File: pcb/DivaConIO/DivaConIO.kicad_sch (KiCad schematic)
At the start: 33 parts, among them J1 DPad Buttons, J10 SWD, J2 Slider i2c, J3 Display i2c, J4 Face Buttons, J5 Button LEDs, J6 L Buttons, J7 Fn Buttons, J8 R Buttons, J9 Slider LEDs, Q1 BC847, Q2 BC847, Q3 BC847, Q4 BC847, SW1 Reset, U1 Pico, U2 SN74LVC1T45DCK

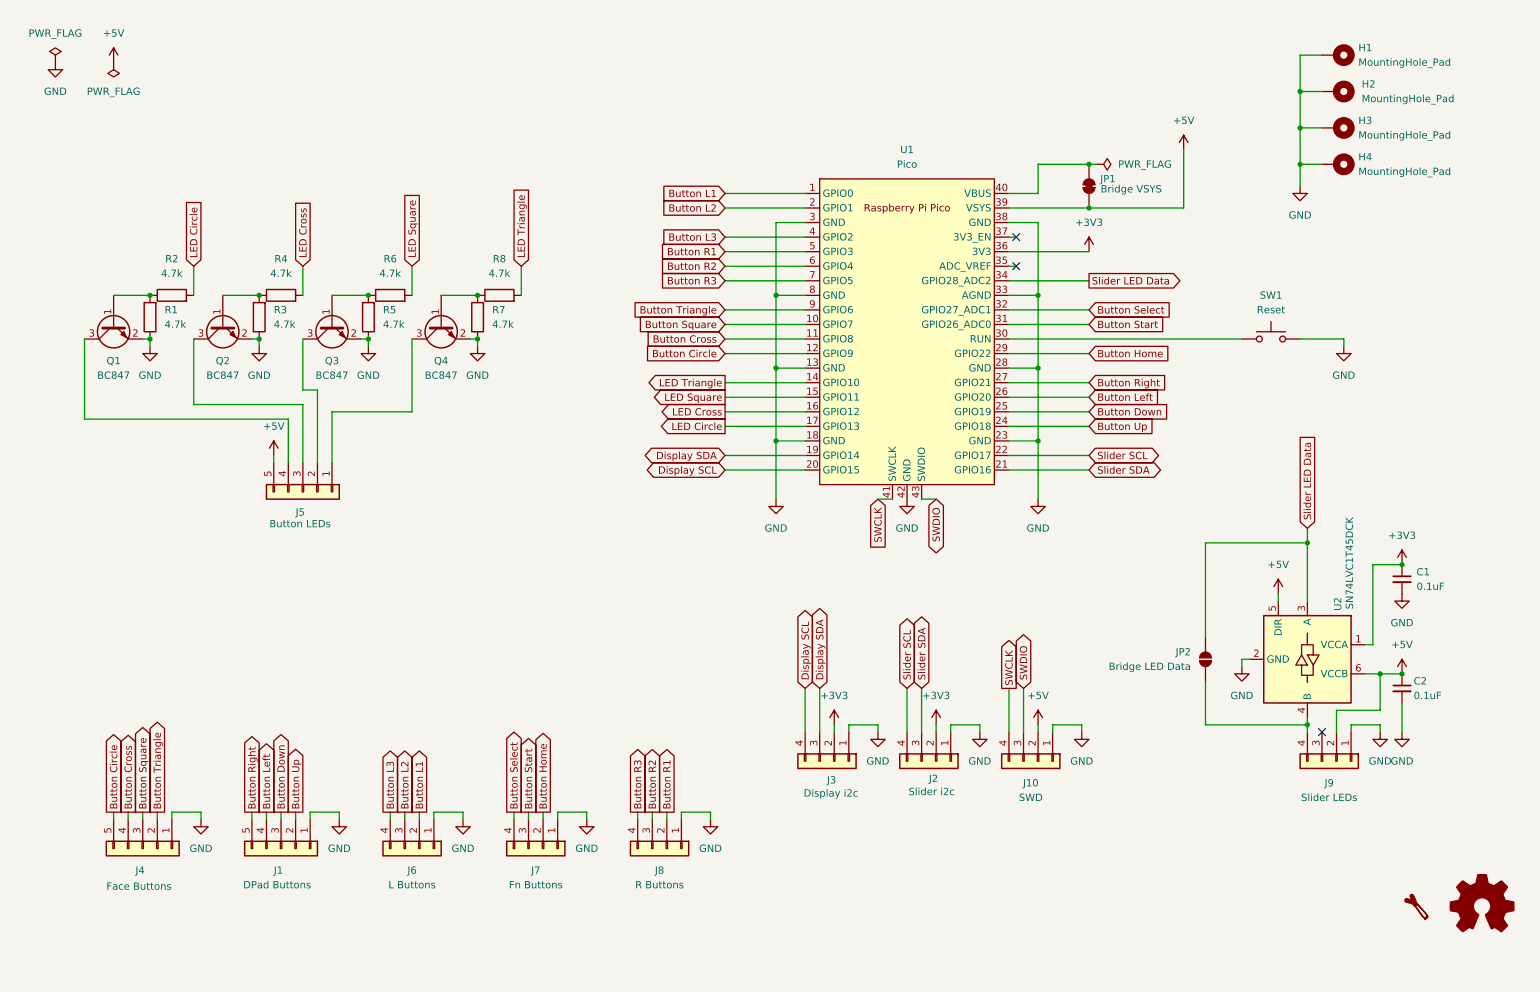
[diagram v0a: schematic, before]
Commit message: relaid out IO board
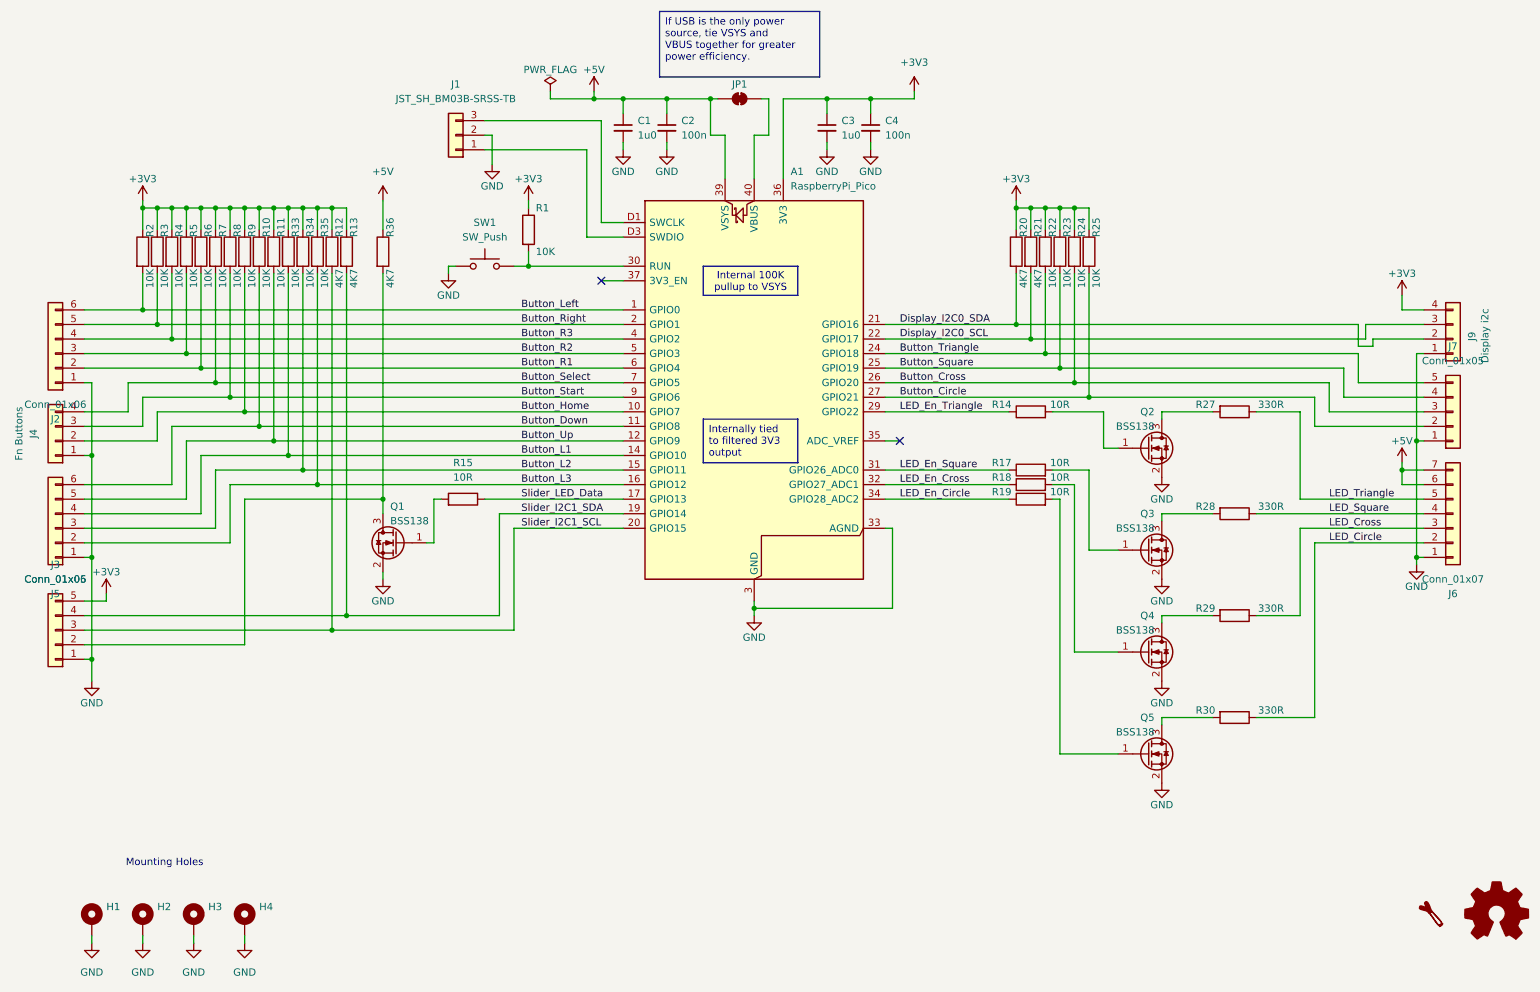
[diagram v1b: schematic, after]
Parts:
- removed J1: DPad Buttons, Connector_JST:JST_PH_B5B-PH-K_1x05_P2.00mm_Vertical, symbol Connector_Generic:Conn_01x05
- removed J10: SWD, Connector_JST:JST_PH_B4B-PH-K_1x04_P2.00mm_Vertical, symbol Connector_Generic:Conn_01x04
- removed J2: Slider i2c, Connector_JST:JST_PH_B4B-PH-K_1x04_P2.00mm_Vertical, symbol Connector_Generic:Conn_01x04
- removed J4: Face Buttons, Connector_JST:JST_PH_B5B-PH-K_1x05_P2.00mm_Vertical, symbol Connector_Generic:Conn_01x05
- removed J5: Button LEDs, Connector_JST:JST_PH_B5B-PH-K_1x05_P2.00mm_Vertical, symbol Connector_Generic:Conn_01x05
- removed J6: L Buttons, Connector_JST:JST_PH_B4B-PH-K_1x04_P2.00mm_Vertical, symbol Connector_Generic:Conn_01x04
- removed J7: Fn Buttons, Connector_JST:JST_PH_B4B-PH-K_1x04_P2.00mm_Vertical, symbol Connector_Generic:Conn_01x04
- removed J8: R Buttons, Connector_JST:JST_PH_B4B-PH-K_1x04_P2.00mm_Vertical, symbol Connector_Generic:Conn_01x04
- removed J9: Slider LEDs, Connector_JST:JST_PH_B4B-PH-K_1x04_P2.00mm_Vertical, symbol Connector_Generic:Conn_01x04
- removed JP2: Bridge LED Data, Jumper:SolderJumper-2_P1.3mm_Open_RoundedPad1.0x1.5mm, symbol Jumper:SolderJumper_2_Open
- removed Q1, Q2, Q3, Q4: BC847, Package_TO_SOT_SMD:SOT-23, symbol Transistor_BJT:BC847
- removed U1: Pico, DivaConIO:RPi_Pico_SMD_TH, symbol DivaConIO:Pico
- removed U2: SN74LVC1T45DCK, Package_TO_SOT_SMD:SOT-363_SC-70-6_Handsoldering, symbol Logic_LevelTranslator:SN74LVC1T45DCK
- added A1: RaspberryPi_Pico, Module:RaspberryPi_Pico_SMD_HandSolder, symbol MCU_Module:RaspberryPi_Pico_Debug
- added C3: 1u0, Capacitor_SMD:C_0603_1608Metric, symbol Device:C_Small
- added C4: 100n, Capacitor_SMD:C_0603_1608Metric, symbol Device:C_Small
- added J1: JST_SH_BM03B-SRSS-TB, Connector_JST:JST_SH_BM03B-SRSS-TB_1x03-1MP_P1.00mm_Vertical, symbol Connector_Generic:Conn_01x03
- added J2, J5: Conn_01x06, Connector_JST:JST_PH_B6B-PH-SM4-TB_1x06-1MP_P2.00mm_Vertical, symbol Connector_Generic:Conn_01x06
- added J3, J7: Conn_01x05, Connector_JST:JST_PH_B5B-PH-SM4-TB_1x05-1MP_P2.00mm_Vertical, symbol Connector_Generic:Conn_01x05
- added J4: Fn Buttons, Connector_JST:JST_PH_B4B-PH-SM4-TB_1x04-1MP_P2.00mm_Vertical, symbol Connector_Generic:Conn_01x04
- added J6: Conn_01x07, Connector_JST:JST_PH_B7B-PH-SM4-TB_1x07-1MP_P2.00mm_Vertical, symbol Connector_Generic:Conn_01x07
- added Q1, Q2, Q3, Q4, Q5: BSS138, Package_TO_SOT_SMD:SOT-23, symbol Transistor_FET:BSS138
- added R10, R11, R22, R23, R24, R25, R33, R34, R35, R9: 10K, Resistor_SMD:R_0603_1608Metric, symbol Device:R
- added R12, R13, R20, R21, R36: 4K7, Resistor_SMD:R_0603_1608Metric, symbol Device:R
- added R14, R15, R17, R18, R19: 10R, Resistor_SMD:R_0603_1608Metric, symbol Device:R
- added R27, R28, R29, R30: 330R, Resistor_SMD:R_0603_1608Metric, symbol Device:R
- C1: value 0.1uF -> 1u0; footprint Capacitor_SMD:C_0805_2012Metric_Pad1.18x1.45mm_HandSolder -> Capacitor_SMD:C_0603_1608Metric
- C2: value 0.1uF -> 100n; footprint Capacitor_SMD:C_0805_2012Metric_Pad1.18x1.45mm_HandSolder -> Capacitor_SMD:C_0603_1608Metric
- H1, H2, H3, H4: footprint MountingHole:MountingHole_4.5mm_Pad_TopOnly -> MountingHole:MountingHole_3.2mm_M3_Pad_Via
- J9: renamed from J3; footprint Connector_JST:JST_PH_B4B-PH-K_1x04_P2.00mm_Vertical -> Connector_JST:JST_PH_B4B-PH-SM4-TB_1x04-1MP_P2.00mm_Vertical
- JP1: value Bridge VSYS -> SolderJumper_2_Bridged
- R1, R2, R3, R4, R5, R6, R7, R8: value 4.7k -> 10K; footprint Resistor_SMD:R_0805_2012Metric_Pad1.20x1.40mm_HandSolder -> Resistor_SMD:R_0603_1608Metric
- SW1: value Reset -> SW_Push; footprint Button_Switch_THT:SW_PUSH_6mm -> Button_Switch_SMD:SW_Push_SPST_NO_Alps_SKRK
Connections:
- net Display SCL is gone; now on net +3V3: J9.4 (Pin_4)
- net +3V3: now also R1.1, R2.1, R3.1, R4.1, R5.1, R6.1, R7.1, R8.1, A1.36 (3V3), C3.1, C4.1, J3.5 (Pin_5), R10.1, R11.1, R12.1, R13.1, R20.1, R21.1, R22.1, R23.1, R24.1, R25.1, R33.1, R34.1, R35.1, R9.1; no longer C1.1, J9.2 (Pin_2)
- net +5V: now also C1.1, A1.39 (VSYS), J6.6 (Pin_6), J6.7 (Pin_7), R36.1
- net GND: now also SW1.1, A1.13 (GND), A1.18 (GND), A1.23 (GND), A1.28 (GND), A1.3 (GND), A1.33 (AGND), A1.38 (GND), A1.8 (GND), A1.D2 (GND), C3.2, C4.2, J1.2 (Pin_2), J2.1 (Pin_1), J3.1 (Pin_1), J4.1 (Pin_1), J5.1 (Pin_1), J6.1 (Pin_1), J7.1 (Pin_1), Q1.2 (S), Q2.2 (S), Q3.2 (S), Q4.2 (S), Q5.2 (S); no longer R1.1, R3.1, R5.1, R7.1, SW1.2
- net at JP1.2 (B): now also A1.40 (VBUS)
- net Button_Right: now reaches R3.2
- net Button_Right: now also A1.2 (GPIO1), J2.5 (Pin_5); no longer R4.1
- net Button_R2: now reaches R5.2
- net Button_R2: now also A1.5 (GPIO3), J2.3 (Pin_3); no longer R6.1
- net at R1.2: now also SW1.2, A1.30 (RUN); no longer R2.1
- net Button_Select: now reaches R7.2
- net Button_Select: now also A1.7 (GPIO5), J4.4 (Pin_4); no longer R8.1
- net Display SDA renamed Display_I2C0_SCL
- net Display_I2C0_SCL: now also A1.22 (GPIO17), R21.2
- net LED Circle renamed Button_Left
- net Button_Left: now also A1.1 (GPIO0), J2.6 (Pin_6)
- net LED Cross renamed Button_R3
- net Button_R3: now also A1.4 (GPIO2), J2.4 (Pin_4)
- net LED Square renamed Button_R1
- net Button_R1: now also A1.6 (GPIO4), J2.2 (Pin_2)
- net LED Triangle renamed Button_Start
- net Button_Start: now also A1.9 (GPIO6), J4.3 (Pin_3)
- new net: Q4.1 (G), R18.2
- new net: Q4.3 (D), R29.2
- new net: Q3.1 (G), R17.2
- new net: Q3.3 (D), R28.2
- new net: Q1.1 (G), R15.2
- new net: J3.2 (Pin_2), Q1.3 (D), R36.2
- new net: Q2.1 (G), R14.2
- new net: Q2.3 (D), R27.2
- new net: A1.D3 (SWDIO), J1.1 (Pin_1)
- new net: A1.D1 (SWCLK), J1.3 (Pin_3)
- new net: Q5.1 (G), R19.2
- new net: Q5.3 (D), R30.2
- new net Button_Circle: A1.27 (GPIO21), J7.2 (Pin_2), R25.2
- new net Button_Cross: A1.26 (GPIO20), J7.3 (Pin_3), R24.2
- new net Button_Down: A1.11 (GPIO8), J5.6 (Pin_6), R10.2
- new net Button_Home: A1.10 (GPIO7), J4.2 (Pin_2), R9.2
- new net Button_L1: A1.14 (GPIO10), J5.4 (Pin_4), R33.2
- new net Button_L2: A1.15 (GPIO11), J5.3 (Pin_3), R34.2
- new net Button_L3: A1.16 (GPIO12), J5.2 (Pin_2), R35.2
- new net Button_Square: A1.25 (GPIO19), J7.4 (Pin_4), R23.2
- new net Button_Triangle: A1.24 (GPIO18), J7.5 (Pin_5), R22.2
- new net Button_Up: A1.12 (GPIO9), J5.5 (Pin_5), R11.2
- new net Display_I2C0_SDA: A1.21 (GPIO16), J9.2 (Pin_2), R20.2
- new net LED_Circle: J6.2 (Pin_2), R30.1
- new net LED_Cross: J6.3 (Pin_3), R29.1
- new net LED_En_Circle: A1.34 (GPIO28_ADC2), R19.1
- new net LED_En_Cross: A1.32 (GPIO27_ADC1), R18.1
- new net LED_En_Square: A1.31 (GPIO26_ADC0), R17.1
- new net LED_En_Triangle: A1.29 (GPIO22), R14.1
- new net LED_Square: J6.4 (Pin_4), R28.1
- new net LED_Triangle: J6.5 (Pin_5), R27.1
- new net Slider_I2C1_SCL: A1.20 (GPIO15), J3.3 (Pin_3), R12.2
- new net Slider_I2C1_SDA: A1.19 (GPIO14), J3.4 (Pin_4), R13.2
- new net Slider_LED_Data: A1.17 (GPIO13), R15.1
- no-connect marks 3 -> 2
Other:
- note added: "Mounting Holes"
- company: ravinrabbid -> Alexander Knapik
- moved on the sheet: J9

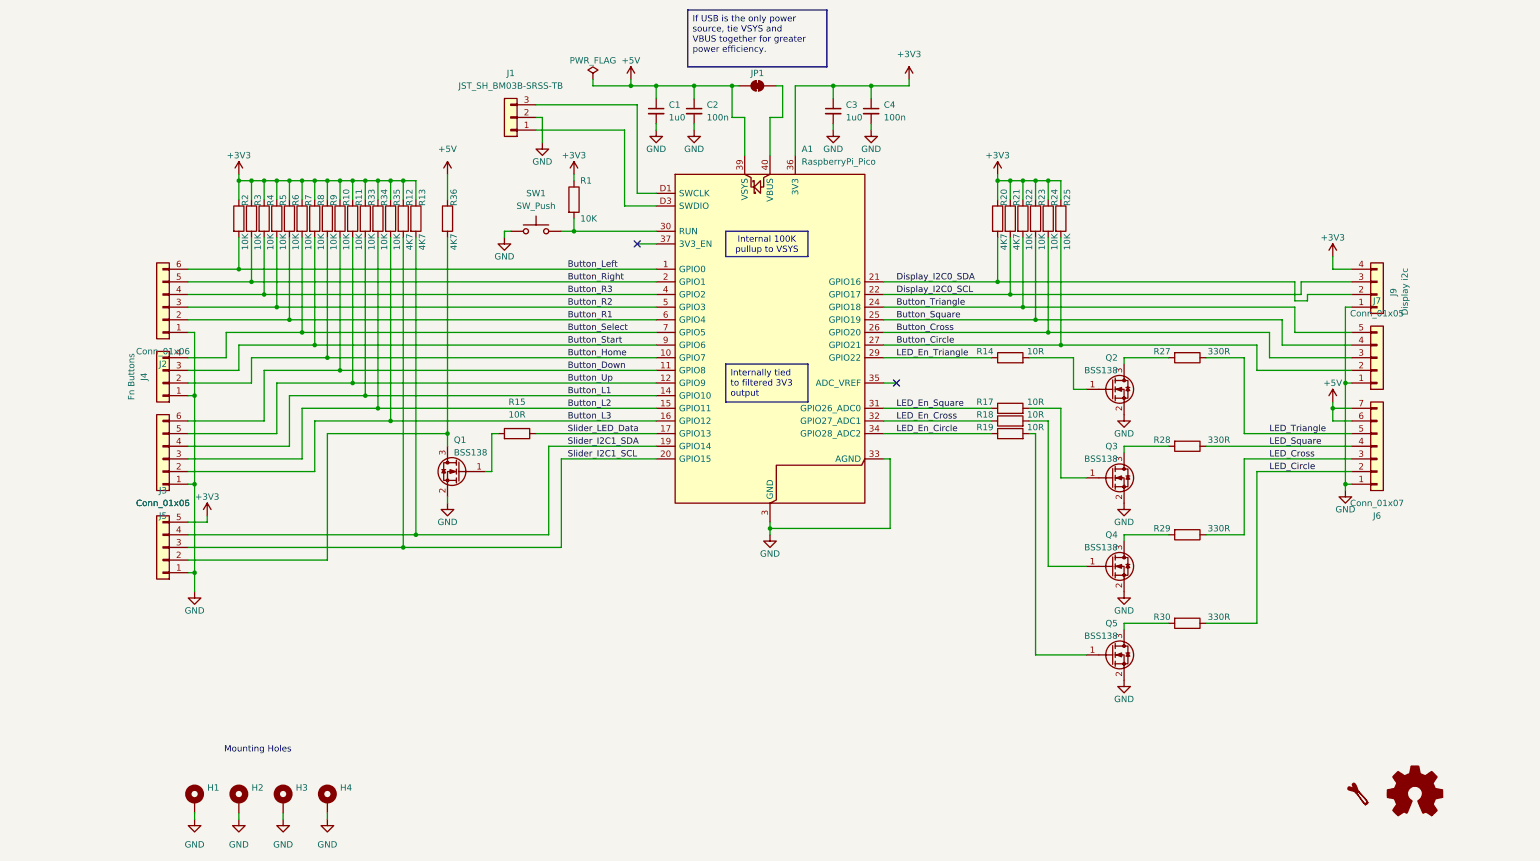
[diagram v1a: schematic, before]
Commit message: placing both I2C buses on the same connector
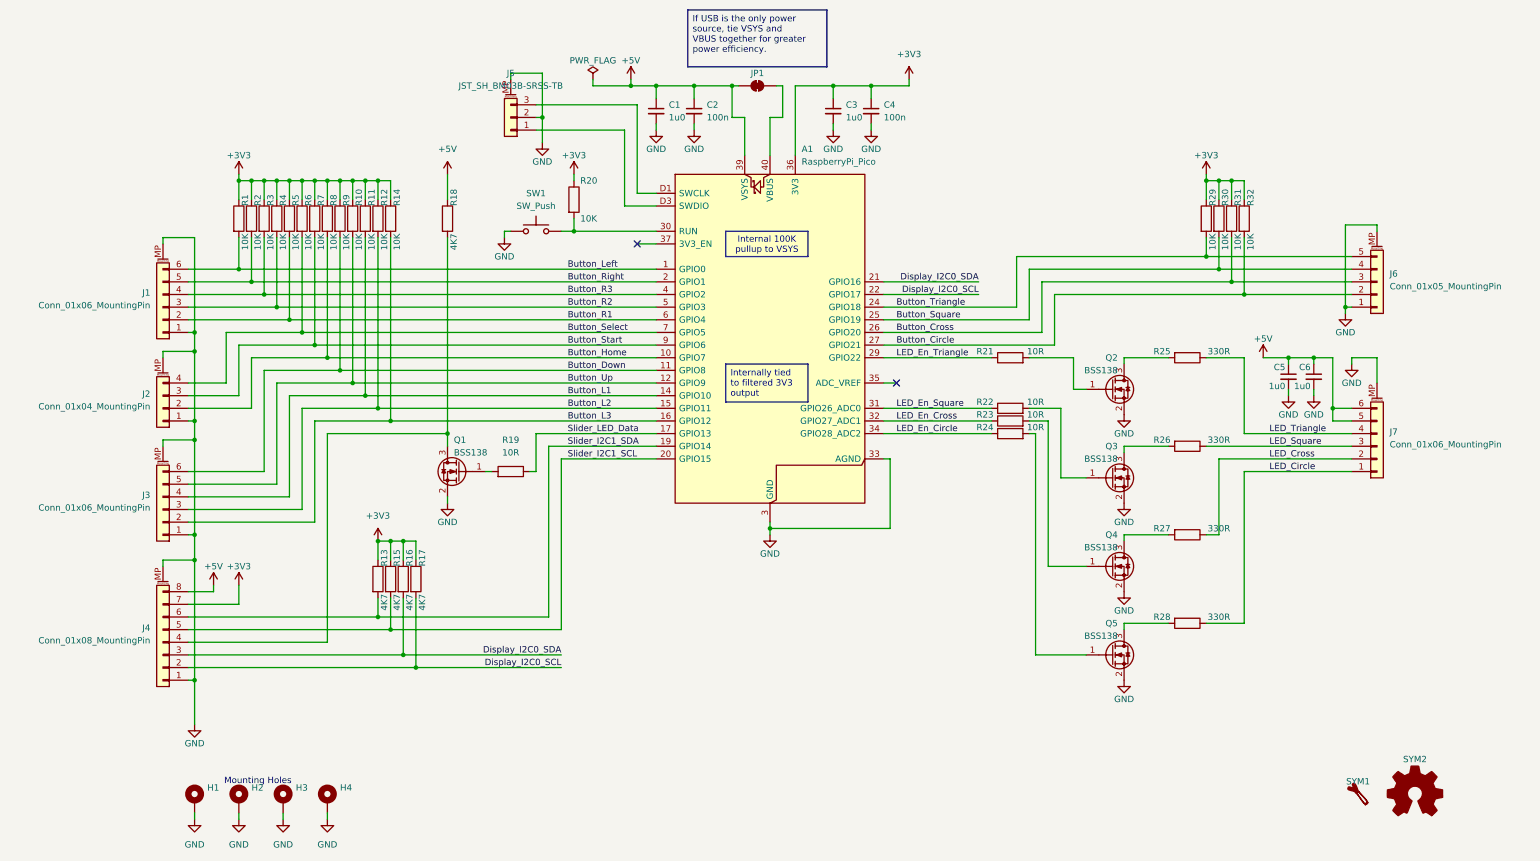
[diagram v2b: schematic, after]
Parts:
- removed J2, J5: Conn_01x06, Connector_JST:JST_PH_B6B-PH-SM4-TB_1x06-1MP_P2.00mm_Vertical, symbol Connector_Generic:Conn_01x06
- removed J3, J7: Conn_01x05, Connector_JST:JST_PH_B5B-PH-SM4-TB_1x05-1MP_P2.00mm_Vertical, symbol Connector_Generic:Conn_01x05
- removed J4: Fn Buttons, Connector_JST:JST_PH_B4B-PH-SM4-TB_1x04-1MP_P2.00mm_Vertical, symbol Connector_Generic:Conn_01x04
- removed J6: Conn_01x07, Connector_JST:JST_PH_B7B-PH-SM4-TB_1x07-1MP_P2.00mm_Vertical, symbol Connector_Generic:Conn_01x07
- removed J9: Display i2c, Connector_JST:JST_PH_B4B-PH-SM4-TB_1x04-1MP_P2.00mm_Vertical, symbol Connector_Generic:Conn_01x04
- removed R12, R20, R21: 4K7, Resistor_SMD:R_0603_1608Metric, symbol Device:R
- added C5, C6: 1u0, Capacitor_SMD:C_0603_1608Metric, symbol Device:C_Small
- added J1, J3, J7: Conn_01x06_MountingPin, Connector_JST:JST_PH_B6B-PH-SM4-TB_1x06-1MP_P2.00mm_Vertical, symbol Connector_Generic_MountingPin:Conn_01x06_MountingPin
- added J2: Conn_01x04_MountingPin, Connector_JST:JST_PH_B4B-PH-SM4-TB_1x04-1MP_P2.00mm_Vertical, symbol Connector_Generic_MountingPin:Conn_01x04_MountingPin
- added J4: Conn_01x08_MountingPin, Connector_JST:JST_PH_B8B-PH-SM4-TB_1x08-1MP_P2.00mm_Vertical, symbol Connector_Generic_MountingPin:Conn_01x08_MountingPin
- added J6: Conn_01x05_MountingPin, Connector_JST:JST_PH_B5B-PH-SM4-TB_1x05-1MP_P2.00mm_Vertical, symbol Connector_Generic_MountingPin:Conn_01x05_MountingPin
- added R15, R16, R17: 4K7, Resistor_SMD:R_0603_1608Metric, symbol Device:R
- added SYM1: Leek, CustomLogos:Leek-Logo_6.3mm_Silkscreen, symbol CustomLogos:Leek
- added SYM2: Logo_Open_Hardware_Small, Symbol:OSHW-Logo2_7.3x6mm_SilkScreen, symbol Graphic:Logo_Open_Hardware_Small
- J5: renamed from J1; symbol Connector_Generic:Conn_01x03 -> Connector_Generic_MountingPin:Conn_01x03_MountingPin
- renumbered R2 to R1, R11 to R10, R33 to R11, R34 to R12, R35 to R14, R36 to R18, R15 to R19, R3 to R2, R1 to R20, R14 to R21, R17 to R22, R18 to R23, R19 to R24, R27 to R25, R28 to R26, R29 to R27, R30 to R28, R22 to R29, R4 to R3, R23 to R30, R24 to R31, R25 to R32, R5 to R4, R6 to R5, R7 to R6, R8 to R7, R9 to R8, R10 to R9
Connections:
- net +3V3: now also J4.7 (Pin_7), R15.1, R16.1, R17.1
- net +5V: now also C5.1, C6.1, J4.8 (Pin_8), J7.5 (Pin_5), J7.6 (Pin_6)
- net Button_Circle: now also J6.2 (Pin_2)
- net Button_Cross: now also J6.3 (Pin_3)
- net Button_Down: now also J3.6 (Pin_6)
- net Button_Home: now also J2.2 (Pin_2)
- net Button_L1: now also J3.4 (Pin_4)
- net Button_L2: now also J3.3 (Pin_3)
- net Button_L3: now also J3.2 (Pin_2)
- net Button_Left: now also J1.6 (Pin_6)
- net Button_R1: now also J1.2 (Pin_2)
- net Button_R2: now also J1.3 (Pin_3)
- net Button_R3: now also J1.4 (Pin_4)
- net Button_Right: now also J1.5 (Pin_5)
- net Button_Select: now also J2.4 (Pin_4)
- net Button_Square: now also J6.4 (Pin_4)
- net Button_Start: now also J2.3 (Pin_3)
- net Button_Triangle: now also J6.5 (Pin_5)
- net Button_Up: now also J3.5 (Pin_5)
- net Display_I2C0_SCL: now also J4.2 (Pin_2), R17.2
- net Display_I2C0_SDA: now also J4.3 (Pin_3), R16.2
- net GND: now also J5.MP (MountPin), C5.2, C6.2, J1.1 (Pin_1), J1.MP (MountPin), J2.1 (Pin_1), J2.MP (MountPin), J3.1 (Pin_1), J3.MP (MountPin), J4.1 (Pin_1), J4.MP (MountPin), J6.1 (Pin_1), J6.MP (MountPin), J7.MP (MountPin)
- net LED_Circle: now also J7.1 (Pin_1)
- net LED_Cross: now also J7.2 (Pin_2)
- net LED_Square: now also J7.3 (Pin_3)
- net LED_Triangle: now also J7.4 (Pin_4)
- net Slider_I2C1_SCL: now also J4.5 (Pin_5), R15.2
- net Slider_I2C1_SDA: now also J4.6 (Pin_6)
- net at Q1.3 (D), R18.2: now also J4.4 (Pin_4)
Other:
- moved on the sheet: R19, R29, R30, R31, R32
